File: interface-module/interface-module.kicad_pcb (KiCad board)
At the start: 2 copper layers, 72.1 x 79.2 mm, 97 parts, among them J2 Conn_01x02, J201 Conn_01x02, J4 Conn_01x08, J6 Conn_01x08, Q201 PMOS, Q202 NMOS, Q203 PMOS, Q204 NMOS, Q205 PMOS, Q206 NMOS, Q207 PMOS, Q208 NMOS, Q209 PMOS, Q210 NMOS, Q211 PMOS, Q212 NMOS, Q213 PMOS, Q214 NMOS, Q215 PMOS, Q216 NMOS, SW1 SW_Coded_SH-7050, U101 MCP3464, U201 140357145200, U202 140357145200, U203 140357145200, U204 140357145200, U205 140357145200, U206 140357145200, U207 140357145200, U208 140357145200, U301 TCA9548

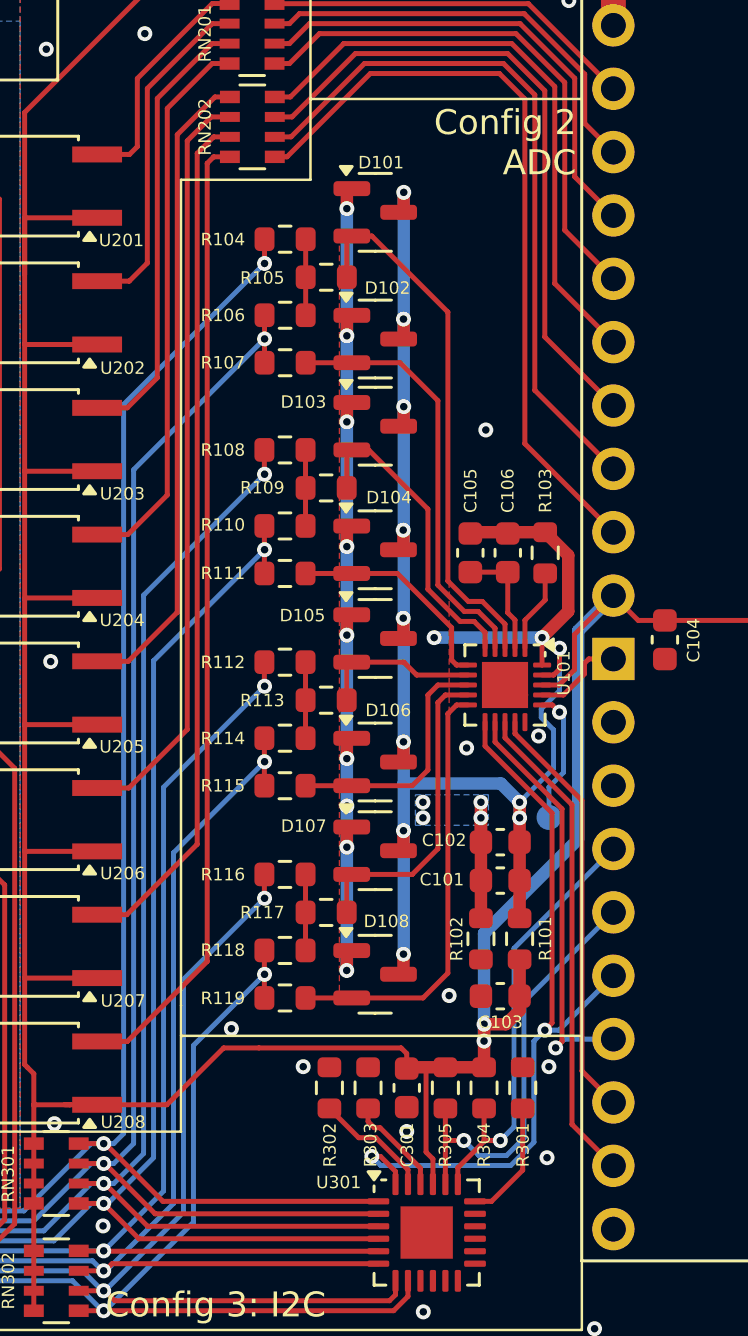
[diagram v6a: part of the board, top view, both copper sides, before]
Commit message: Added ADC biasing resistor
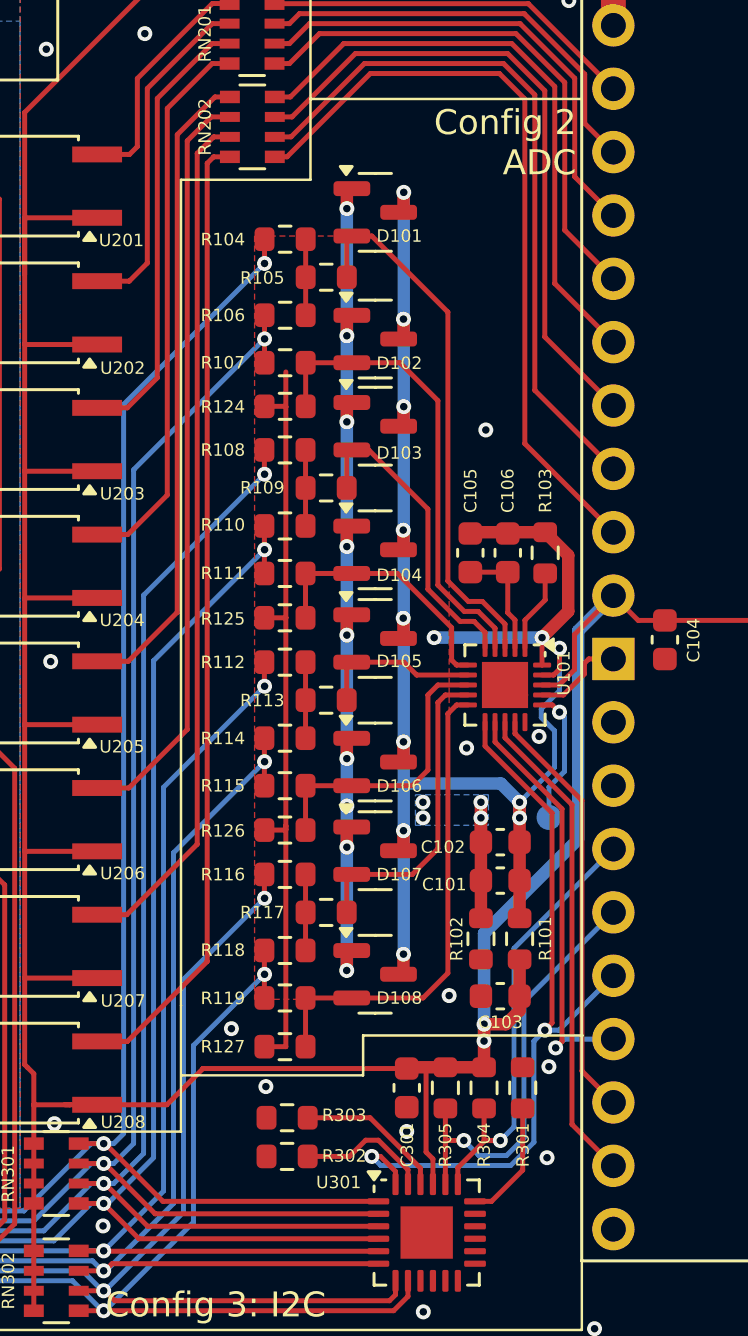
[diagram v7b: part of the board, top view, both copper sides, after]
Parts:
- added R124: R_BIAS, Resistor_SMD:R_0603_1608Metric, F.Cu at (146.2, 104.1)
- added R125: R_BIAS, Resistor_SMD:R_0603_1608Metric, F.Cu at (146.2, 112.6)
- added R126: R_BIAS, Resistor_SMD:R_0603_1608Metric, F.Cu at (146.2, 121.1)
- added R127: R_BIAS, Resistor_SMD:R_0603_1608Metric, F.Cu at (146.2, 129.8)
- moved R303 3.46 mm to (146.2, 132.6), turned to 0 degrees
- moved R302 3.23 mm to (146.2, 134.2), turned to 0 degrees
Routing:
- net GNDA: track 56.1 -> 86.7 mm
- net Net-(U301-A0): track 4.04 -> 6.00 mm
- net IN3-: track 17.5 -> 19.4 mm
- net IN2-: track 9.94 -> 11.7 mm
- net IN1-: track 8.79 -> 10.6 mm
- net IN0-: track 17.1 -> 18.9 mm
- net +3V3: track 212.9 -> 211.9 mm
- net Net-(U301-A1): track 4.75 -> 5.36 mm

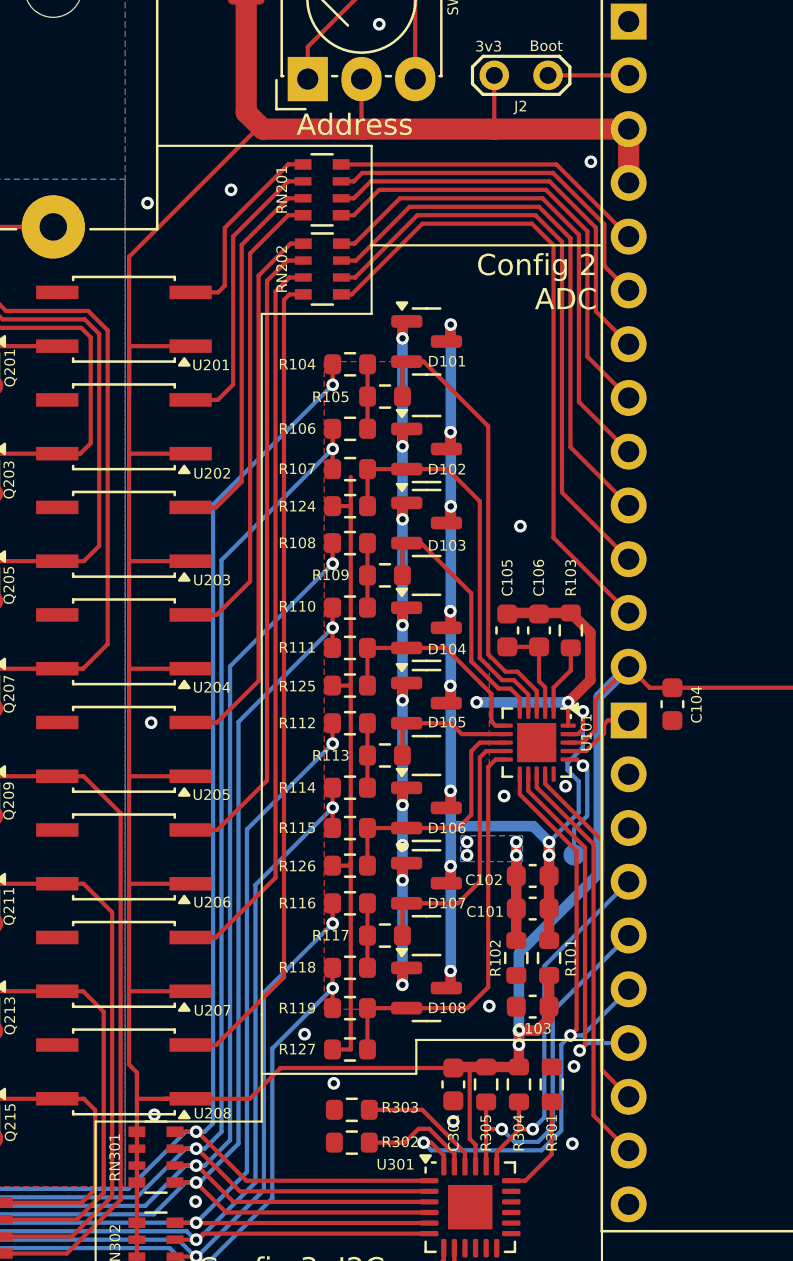
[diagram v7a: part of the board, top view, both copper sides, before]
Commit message: Fixed output polarity
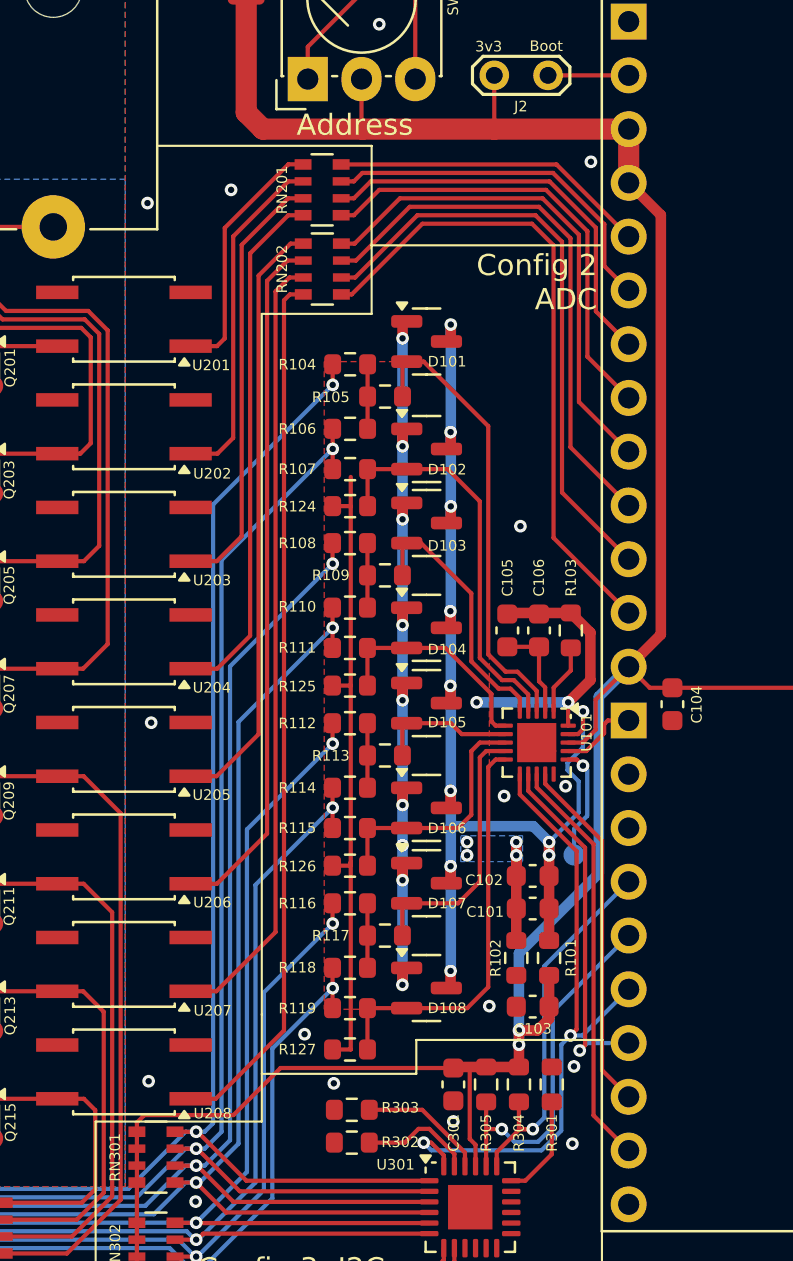
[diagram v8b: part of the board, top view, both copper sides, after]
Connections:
- U201 pad 1: +3V3 -> Net-(RN201A-R1.1)
- U201 pad 2: Net-(RN201A-R1.1) -> GND
- U202 pad 1: +3V3 -> Net-(RN201B-R2.1)
- U202 pad 2: Net-(RN201B-R2.1) -> GND
- U203 pad 1: +3V3 -> Net-(RN201C-R3.1)
- U203 pad 2: Net-(RN201C-R3.1) -> GND
- U204 pad 1: +3V3 -> Net-(RN201D-R4.1)
- U204 pad 2: Net-(RN201D-R4.1) -> GND
- U205 pad 1: +3V3 -> Net-(RN202A-R1.1)
- U205 pad 2: Net-(RN202A-R1.1) -> GND
- U206 pad 1: +3V3 -> Net-(RN202B-R2.1)
- U206 pad 2: Net-(RN202B-R2.1) -> GND
- U207 pad 1: +3V3 -> Net-(RN202C-R3.1)
- U207 pad 2: Net-(RN202C-R3.1) -> GND
- U208 pad 1: +3V3 -> Net-(RN202D-R4.1)
- U208 pad 2: Net-(RN202D-R4.1) -> GND
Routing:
- net +3V3: track 211.9 -> 164.0 mm
- net Net-(RN202C-R3.1): track 34.5 -> 37.0 mm
- net Net-(RN201D-R4.1): track 22.2 -> 24.8 mm
- net Net-(RN201C-R3.1): track 17.9 -> 20.5 mm
- net Net-(RN202B-R2.1): track 30.3 -> 32.8 mm
- net Net-(RN201B-R2.1): track 13.7 -> 16.2 mm
- net Net-(RN202A-R1.1): track 25.9 -> 28.4 mm
- net Net-(RN202D-R4.1): track 38.8 -> 41.3 mm
- net Net-(RN201A-R1.1): track 9.41 -> 11.9 mm
